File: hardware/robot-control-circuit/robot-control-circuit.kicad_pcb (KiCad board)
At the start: 4 copper layers, 181 x 127 mm, 34 parts, among them J1 CCRP5-EC2, J10 Testpoint GND, J11 Testpoint VDD, J12 Testpoint VCC, J13 CCRP5_Injections, J2 VL53L1-SATEL connector 1, J3 VL53L1-SATEL connector 2, J4 CCRP5-EC1, J5 VL53L1-SATEL connector 3, J6 VL53L1-SATEL connector 4, J7 CCRP5-EC3, J8 Bumper, Q1 BD235, Q2 BD235, U1 LM7805_TO220, U2 NodeMCU_1.0_(ESP-12E), U3 MCP23017_SP

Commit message: Added inverter between D0 and !RESET of IO expander.
As in case the IO expander is active during boot, it puts INTB high, which is connected to GPIO15 which shall not be high during boot. Else boot fails.
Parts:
- added Q3: BC548, Package_TO_SOT_THT:TO-92_Inline_Wide, F.Cu at (193.0, 86.4)
- added R16: 10 k, Resistor_THT:R_Axial_DIN0204_L3.6mm_D1.6mm_P2.54mm_Vertical, F.Cu at (190.5, 88.9)
- added R17: 10 k, Resistor_THT:R_Axial_DIN0204_L3.6mm_D1.6mm_P2.54mm_Vertical, F.Cu at (193.0, 78.7)
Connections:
- U2 pad 30: (no net) -> /IO-EXP-1_RESET
- U3 pad 18: /VDD -> /IO-EXP-1_!RESET
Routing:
- net GND: track 452.6 -> 476.0 mm, vias 13 -> 14
- net /IO-EXP-1_RESET: track 0.00 -> 22.0 mm, vias 0 -> 2
- net /VDD: track 313.0 -> 329.5 mm, vias 2 -> 4
- net /IO-EXP-1_!RESET: track 0.00 -> 16.3 mm, vias 0 -> 2
- net /VL53L1-3_INT: track 85.7 -> 73.3 mm, vias 1 -> 3
- net Net-(Q3-Pad2): track 0.00 -> 2.54 mm
- net /IO-EXP-1_INTA: track 62.2 -> 59.9 mm, vias 2 -> 1
- net /IO-EXP-1_INTB: track 62.2 -> 61.6 mm, vias 2 -> 1
- net /VL53L1-3_XSHUT: track 81.5 -> 82.1 mm, vias 2 -> 4

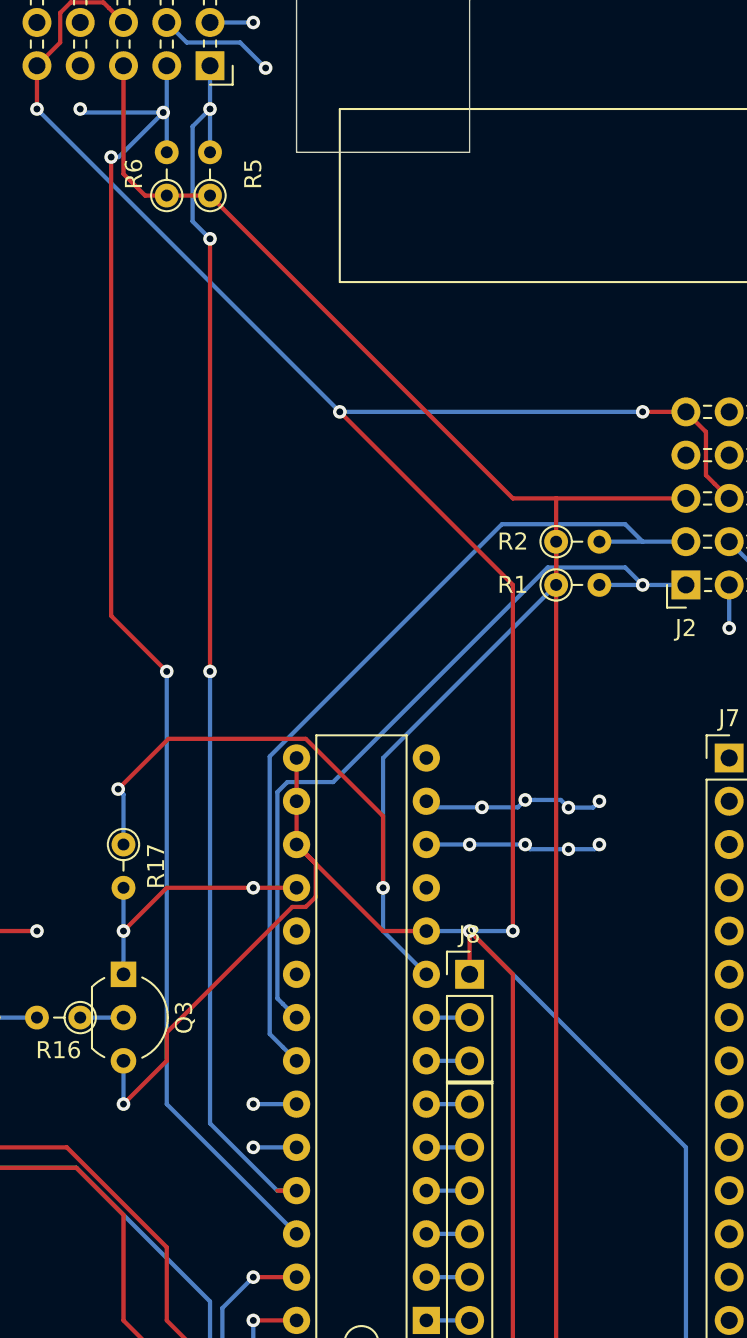
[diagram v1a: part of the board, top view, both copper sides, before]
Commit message: Added capacitors for io-expander.
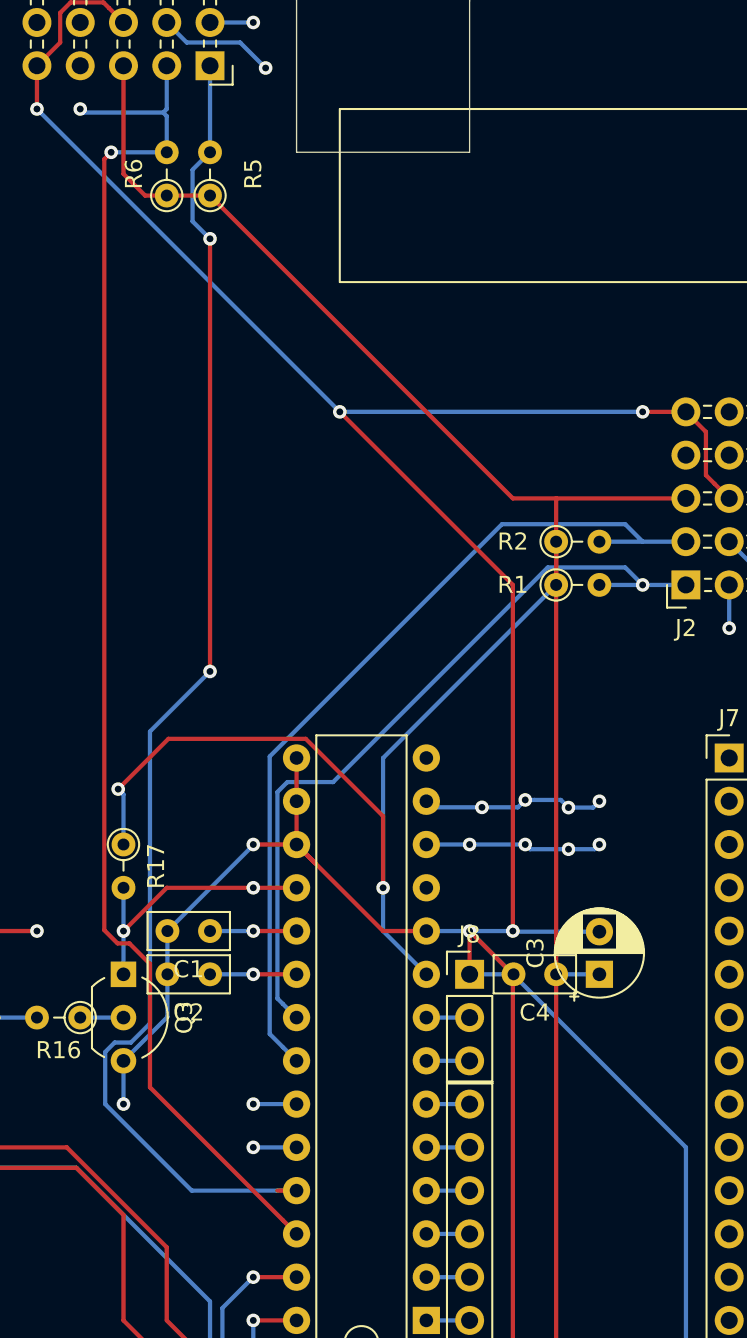
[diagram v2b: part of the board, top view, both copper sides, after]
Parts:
- added C1: 47 n, Capacitor_THT:C_Rect_L4.6mm_W2.0mm_P2.50mm_MKS02_FKP02, F.Cu at (198.1, 83.8)
- added C2: 47 n, Capacitor_THT:C_Rect_L4.6mm_W2.0mm_P2.50mm_MKS02_FKP02, F.Cu at (198.1, 86.4)
- added C3: 10 µ, Capacitor_THT:CP_Radial_D5.0mm_P2.50mm, F.Cu at (221.0, 86.4)
- added C4: 47 n, Capacitor_THT:C_Rect_L4.6mm_W2.0mm_P2.50mm_MKS02_FKP02, F.Cu at (218.4, 86.4)
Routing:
- net GND: track 476.0 -> 482.8 mm, vias 14 -> 15
- net /VL53L1-3_INT: track 73.3 -> 79.4 mm
- net /IO-EXP-1_INTB: track 61.6 -> 66.7 mm, vias 1 -> 2
- net /IO-EXP-1_INTA: track 59.9 -> 65.0 mm, vias 1 -> 2
- net /VDD: track 329.5 -> 332.1 mm
- net /VL53L1-3_XSHUT: track 82.1 -> 82.2 mm, vias 4 -> 2

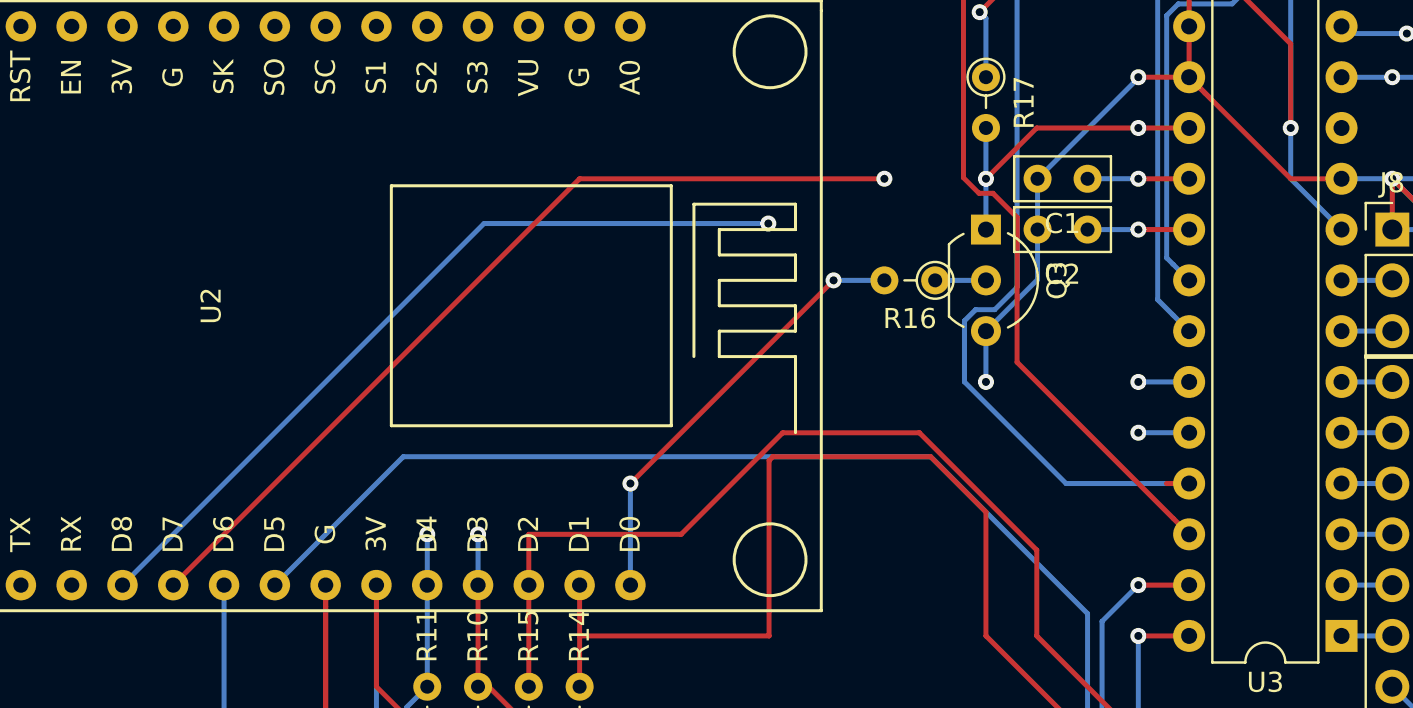
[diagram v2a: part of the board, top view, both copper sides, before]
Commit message: Directly connect !RESET of IO-expander to VDD and invert INTA.
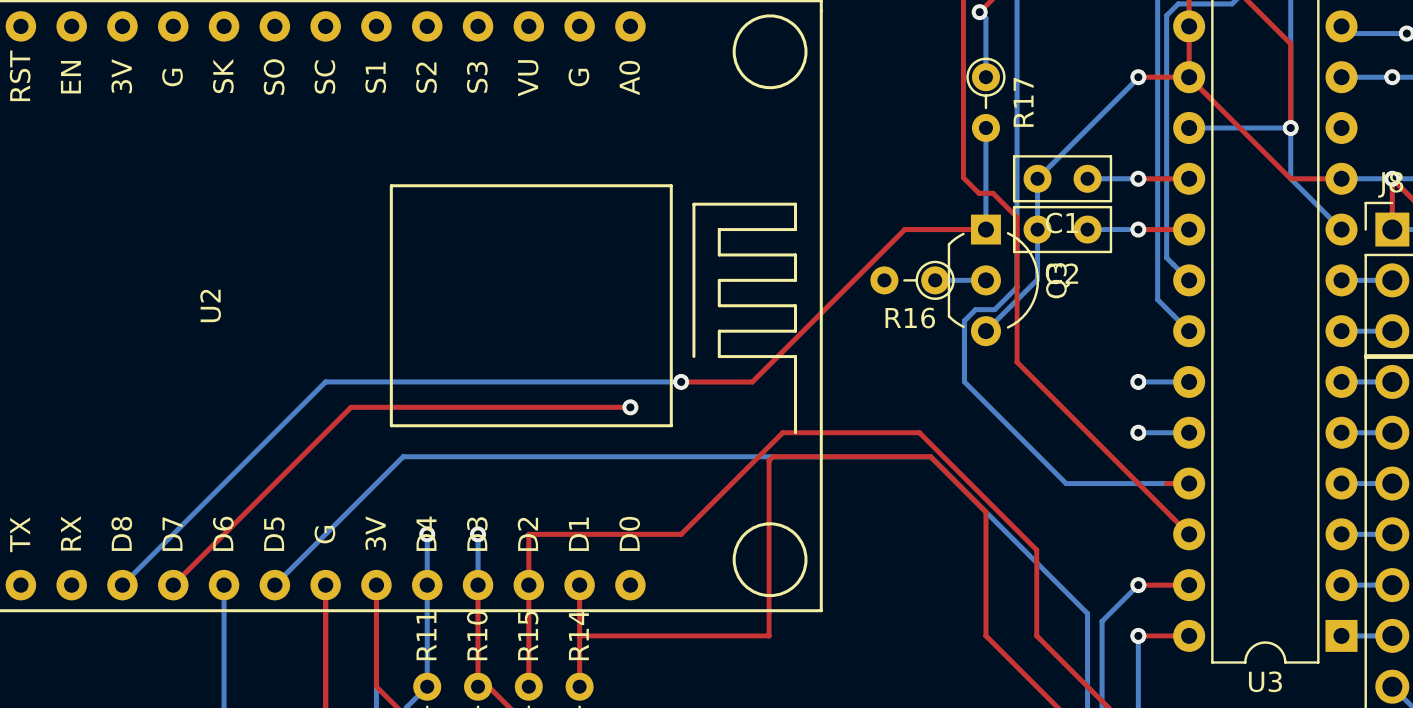
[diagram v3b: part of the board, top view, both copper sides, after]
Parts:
- C1, C2, C4: value 47 n -> 100 n
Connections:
- Q3 pad 1: /IO-EXP-1_!RESET -> /IO-EXP-1_!INTA
- R16 pad 2: /IO-EXP-1_RESET -> /IO-EXP-1_INTA
- R17 pad 2: /IO-EXP-1_!RESET -> /IO-EXP-1_!INTA
- U2 pad 20: /IO-EXP-1_INTB -> /IO-EXP-1_!INTA
- U2 pad 21: /IO-EXP-1_INTA -> /IO-EXP-1_INTB
- U2 pad 30: /IO-EXP-1_RESET -> (no net)
- U3 pad 18: /IO-EXP-1_!RESET -> /VDD
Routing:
- net /IO-EXP-1_!INTA: track 0.00 -> 55.6 mm, vias 0 -> 1
- net /IO-EXP-1_INTA: track 65.0 -> 17.3 mm, vias 2 -> 1
- net /IO-EXP-1_RESET: track 22.0 -> 0.00 mm, vias 2 -> 0
- net /IO-EXP-1_!RESET: track 16.3 -> 0.00 mm, vias 2 -> 0
- net /IO-EXP-1_INTB: track 66.7 -> 59.1 mm
- net /VDD: track 332.1 -> 337.2 mm
- net GND: track 482.8 -> 480.2 mm, vias 15 -> 14

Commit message: Added LEDs for generic signaling purposes.
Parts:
- added D3: Signal LED green, LED_THT:LED_D3.0mm, F.Cu at (148.6, 31.8)
- added D4: Signal LED yellow, LED_THT:LED_D3.0mm, F.Cu at (154.9, 31.8)
- added D5: Signal LED red, LED_THT:LED_D3.0mm, F.Cu at (161.3, 31.8)
- added D6: Signal LED blue, LED_THT:LED_D3.0mm, F.Cu at (167.6, 31.8)
- added R18: 1k, Resistor_THT:R_Axial_DIN0204_L3.6mm_D1.6mm_P2.54mm_Vertical, F.Cu at (148.6, 36.8)
- added R19: 1k, Resistor_THT:R_Axial_DIN0204_L3.6mm_D1.6mm_P2.54mm_Vertical, F.Cu at (154.9, 36.8)
- added R20: 1k, Resistor_THT:R_Axial_DIN0204_L3.6mm_D1.6mm_P2.54mm_Vertical, F.Cu at (161.3, 36.8)
- added R21: 0, Resistor_THT:R_Axial_DIN0204_L3.6mm_D1.6mm_P2.54mm_Vertical, F.Cu at (167.6, 36.8)
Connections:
- net Net-(J13-Pad10) renamed /LED_BLUE
- net Net-(J13-Pad7) renamed /LED_GREEN
- net Net-(J13-Pad8) renamed /LED_YELLOW
- net Net-(J13-Pad9) renamed /LED_RED
- J8 pad 2: /BUMPER_LEFT -> /BUMPER_RIGHT
- J8 pad 3: /BUMPER_RIGHT -> /BUMPER_LEFT
- U3 pad 7: /BUMPER_RIGHT -> /BUMPER_LEFT
- U3 pad 8: /BUMPER_LEFT -> /BUMPER_RIGHT
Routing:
- net GND: track 480.2 -> 520.1 mm
- net Net-(D6-Pad2): track 0.00 -> 2.54 mm
- net Net-(D5-Pad2): track 0.00 -> 2.54 mm
- net Net-(D4-Pad2): track 0.00 -> 2.54 mm
- net Net-(D3-Pad2): track 0.00 -> 2.54 mm

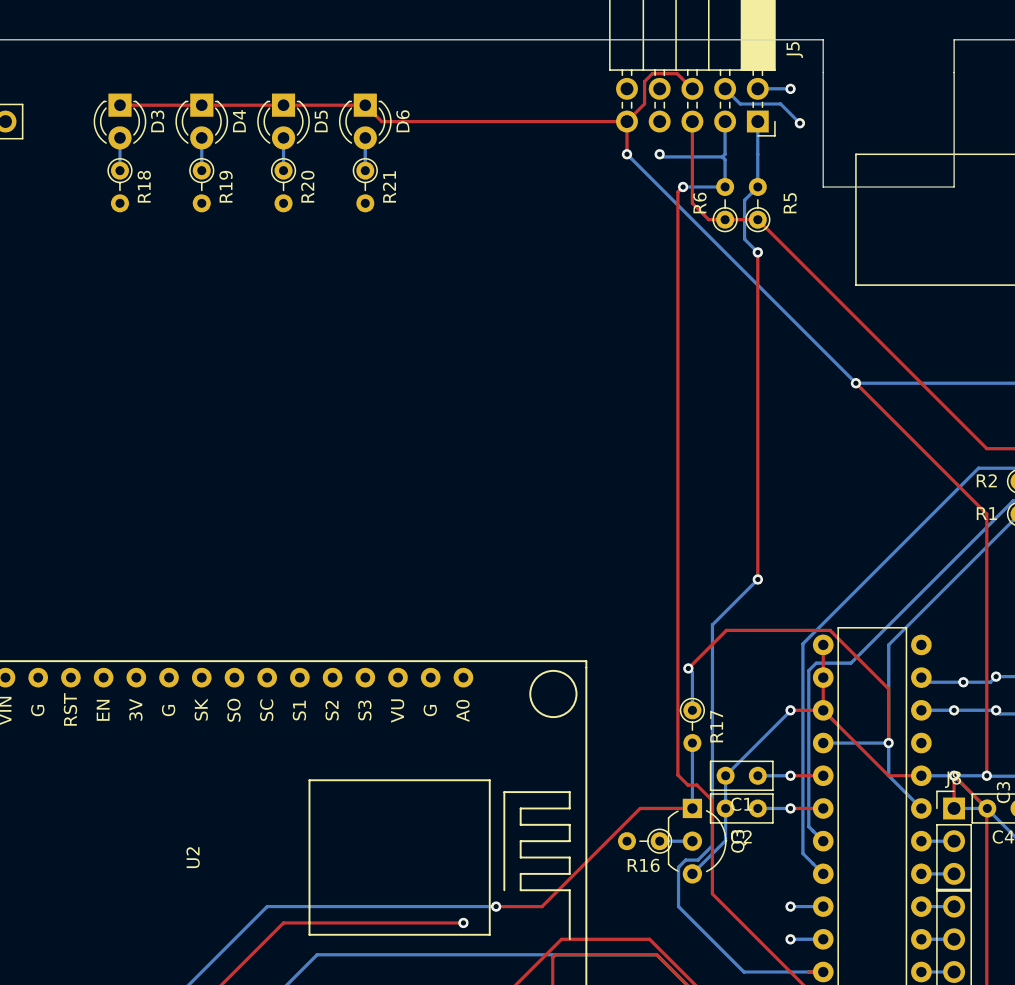
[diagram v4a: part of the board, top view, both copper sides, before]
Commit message: Connected new LEDs.
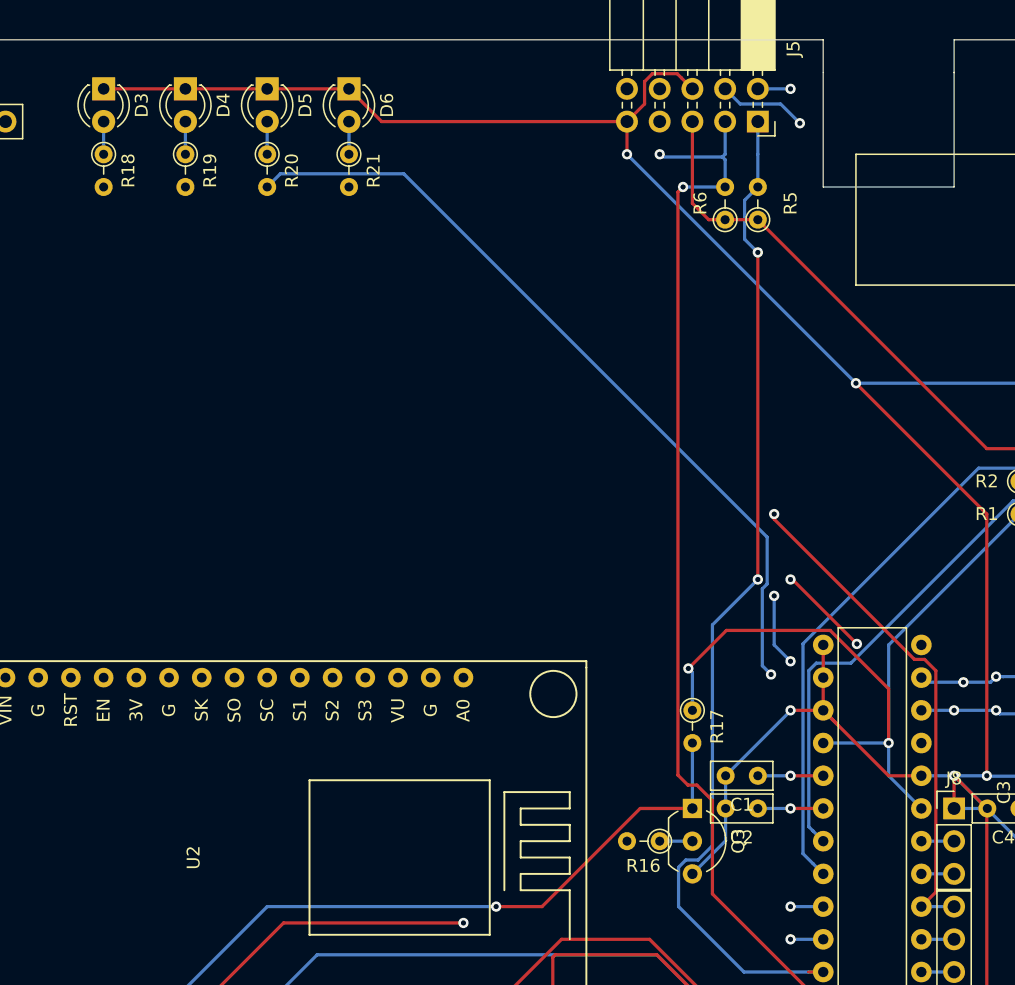
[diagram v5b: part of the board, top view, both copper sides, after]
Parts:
- moved D3 1.80 mm to (147.3, 30.5)
- moved D4 1.80 mm to (153.7, 30.5)
- moved R18 1.80 mm to (147.3, 35.6)
- moved R19 1.80 mm to (153.7, 35.6)
- moved D5 1.80 mm to (160.0, 30.5)
- moved D6 1.80 mm to (166.4, 30.5)
- moved R20 1.80 mm to (160.0, 35.6)
- moved R21 1.80 mm to (166.4, 35.6)
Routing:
- net /LED_GREEN: track 2.54 -> 107.4 mm, vias 0 -> 2
- net /LED_RED: track 2.54 -> 99.5 mm, vias 0 -> 1
- net /LED_YELLOW: track 2.54 -> 97.5 mm, vias 0 -> 2
- net /LED_BLUE: track 2.54 -> 82.7 mm, vias 0 -> 1
- net GND: track 520.1 -> 521.9 mm
